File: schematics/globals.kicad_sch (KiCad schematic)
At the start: 35 parts, among them J1 Power, U1 74HCU04, U2 74HC14, U3 ATF22V10C-7, U4 74HC590, U5 74HC590, U6 74HC590, U7 PicoROM32, Y1 12MHz

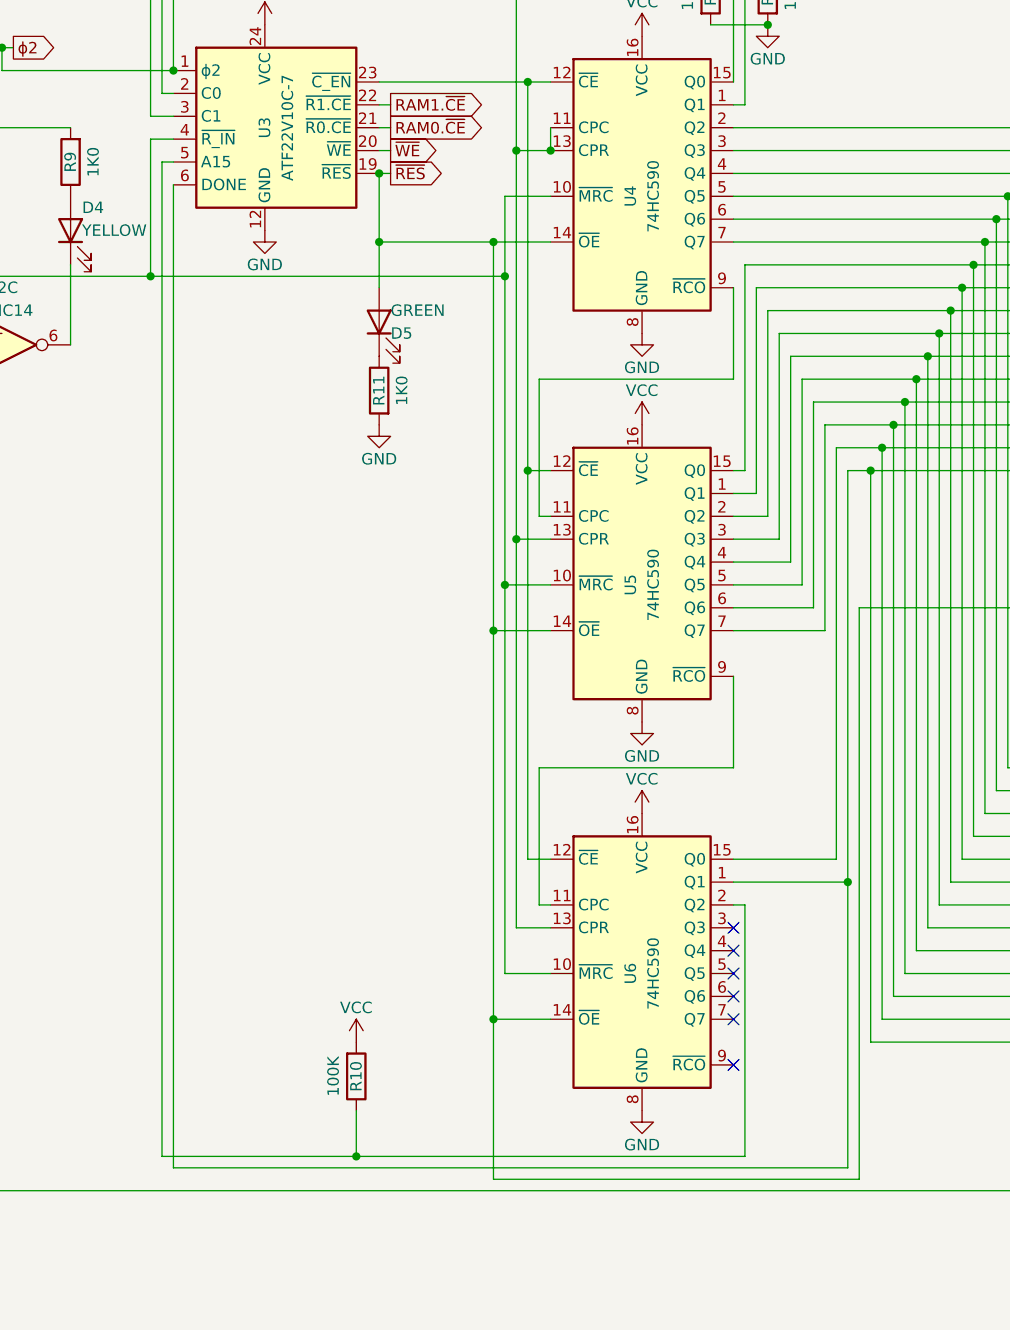
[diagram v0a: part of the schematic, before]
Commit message: forgot bank register transciever so now it's write-only
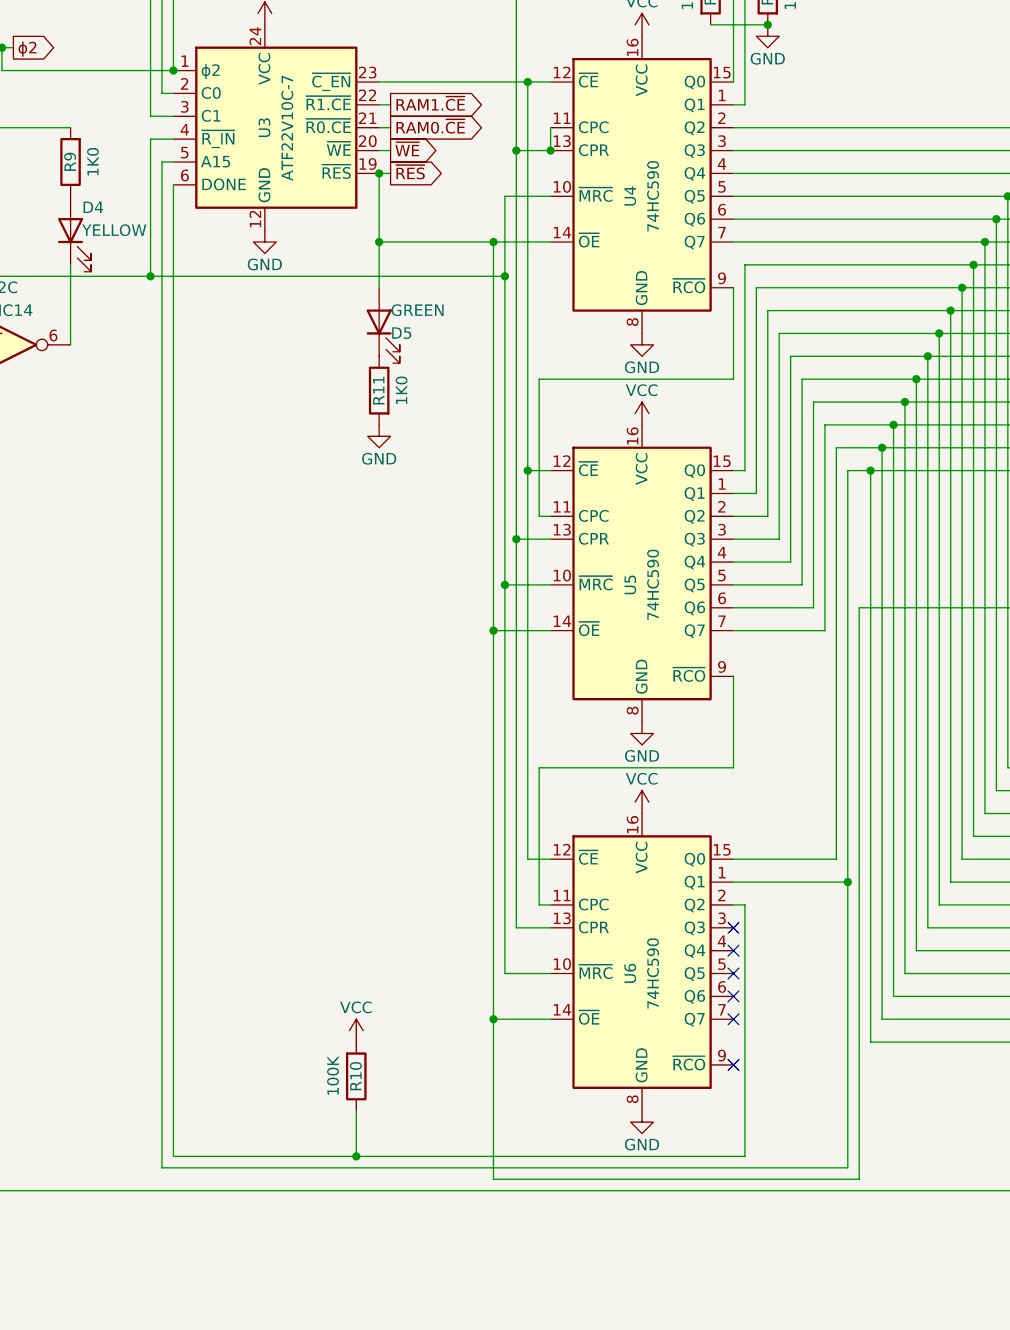
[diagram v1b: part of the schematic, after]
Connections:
- net A15: now also U3.5 (A15); no longer U3.6 (DONE)
- net at R10.1, U6.2 (Q2): now also U3.6 (DONE); no longer U3.5 (A15)
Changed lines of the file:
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@@
 	(wire
 		(pts
-			(xy 116.84 163.83) (xy 191.77 163.83)
+			(xy 115.57 163.83) (xy 191.77 163.83)
 		)
 		(stroke
@@
 	(wire
 		(pts
-			(xy 116.84 54.61) (xy 116.84 163.83)
-		)
-		(stroke
-			(width 0)
-			(type default)
-		)
-	)
-	(wire
-		(pts
 			(xy 59.69 59.69) (xy 59.69 64.77)
 		)
@@
 	(wire
 		(pts
-			(xy 115.57 52.07) (xy 115.57 162.56)
-		)
-		(stroke
-			(width 0)
-			(type default)
-		)
-	)
-	(wire
-		(pts
 			(xy 156.21 86.36) (xy 156.21 43.18)
 		)
@@
 	(wire
 		(pts
+			(xy 115.57 52.07) (xy 116.84 52.07)
+		)
+		(stroke
+			(width 0)
+			(type default)
+		)
+	)
+	(wire
+		(pts
 			(xy 55.88 95.25) (xy 62.23 95.25)
 		)
@@
 	(wire
 		(pts
+			(xy 115.57 52.07) (xy 115.57 163.83)
+		)
+		(stroke
+			(width 0)
+			(type default)
+		)
+	)
+	(wire
+		(pts
 			(xy 191.77 86.36) (xy 194.31 86.36)
 		)
@@
 	(wire
 		(pts
-			(xy 115.57 162.56) (xy 137.16 162.56)
+			(xy 116.84 162.56) (xy 137.16 162.56)
 		)
 		(stroke
@@
 	(wire
 		(pts
+			(xy 116.84 54.61) (xy 116.84 162.56)
+		)
+		(stroke
+			(width 0)
+			(type default)
+		)
+	)
+	(wire
+		(pts
 			(xy 189.23 104.14) (xy 189.23 81.28)
 		)
@@
 		)
 		(stroke
-			(width 0)
-			(type default)
-		)
-	)
-	(wire
-		(pts
-			(xy 116.84 52.07) (xy 115.57 52.07)
-		)
-		(stroke

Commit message: fixing wiring
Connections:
- net A15: now also U3.10 (A15); no longer U3.5 (A15)
- net RAM0.~{CE}: now also U3.16 (R0.~{CE}); no longer U3.21 (~{R0.CE})
- net RAM1.~{CE}: now also U3.17 (R1.~{CE}); no longer U3.22 (~{R1.CE})
- net ~{RES}: now also U3.14 (~{RES}), U3.21
- net ~{WE}: now also U3.15 (~{WE}); no longer U3.20 (~{WE})
- net at R12.1, U4.15 (Q0): now also U3.8 (C0); no longer U3.2 (C0)
- net at R13.1, U4.1 (Q1): now also U3.9 (C1); no longer U3.3 (C1)
- net at D3.2 (A), R6.1, U2.5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: now also U3.7 (~{R_IN}); no longer U3.4 (~{R_IN})
- net at U4.12 (~{CE}), U5.12 (~{CE}), U6.12 (~{CE}): now also U3.18 (C.~{EN}); no longer U3.23 (~{C_EN})
- net at U3.11 (DONE): now also R10.1, U6.2 (Q2)
- now unconnected: U3.6 (DONE)
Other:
- moved on the sheet: C1, C3, R1, R10, R2, R7, R8, U1A, U1B, U1C, U1D, U2A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

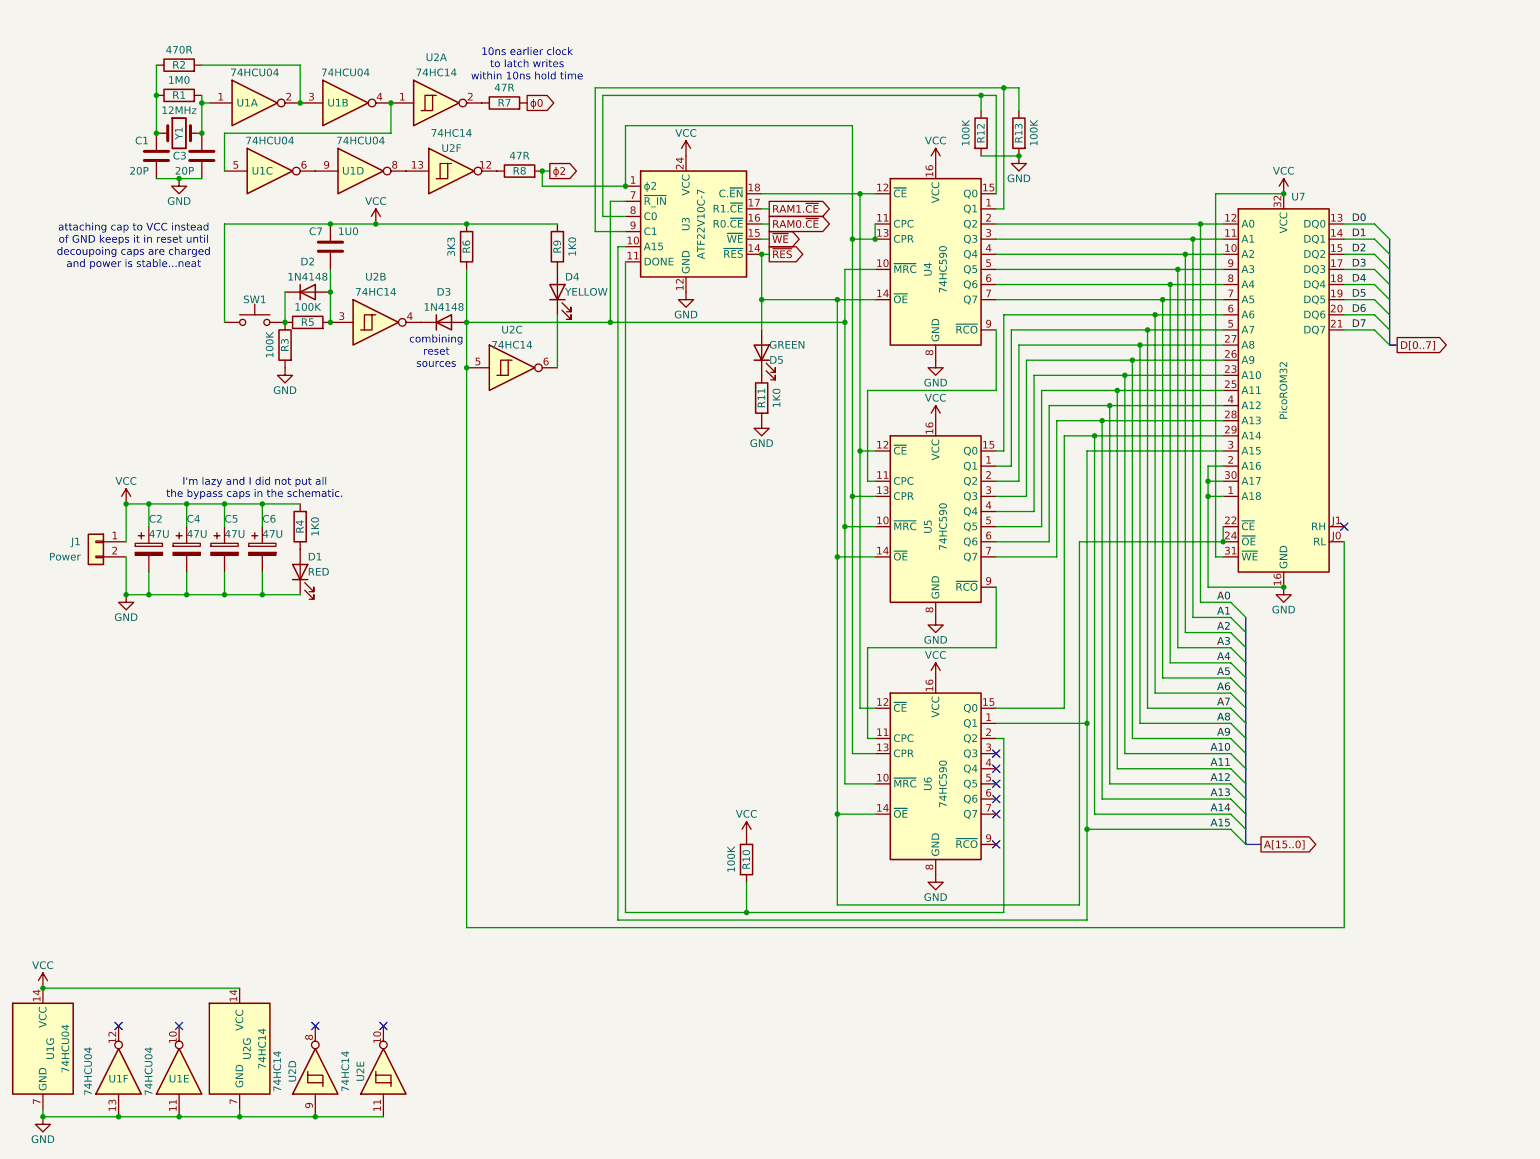
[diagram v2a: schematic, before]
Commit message: combined reset inputs in the pld
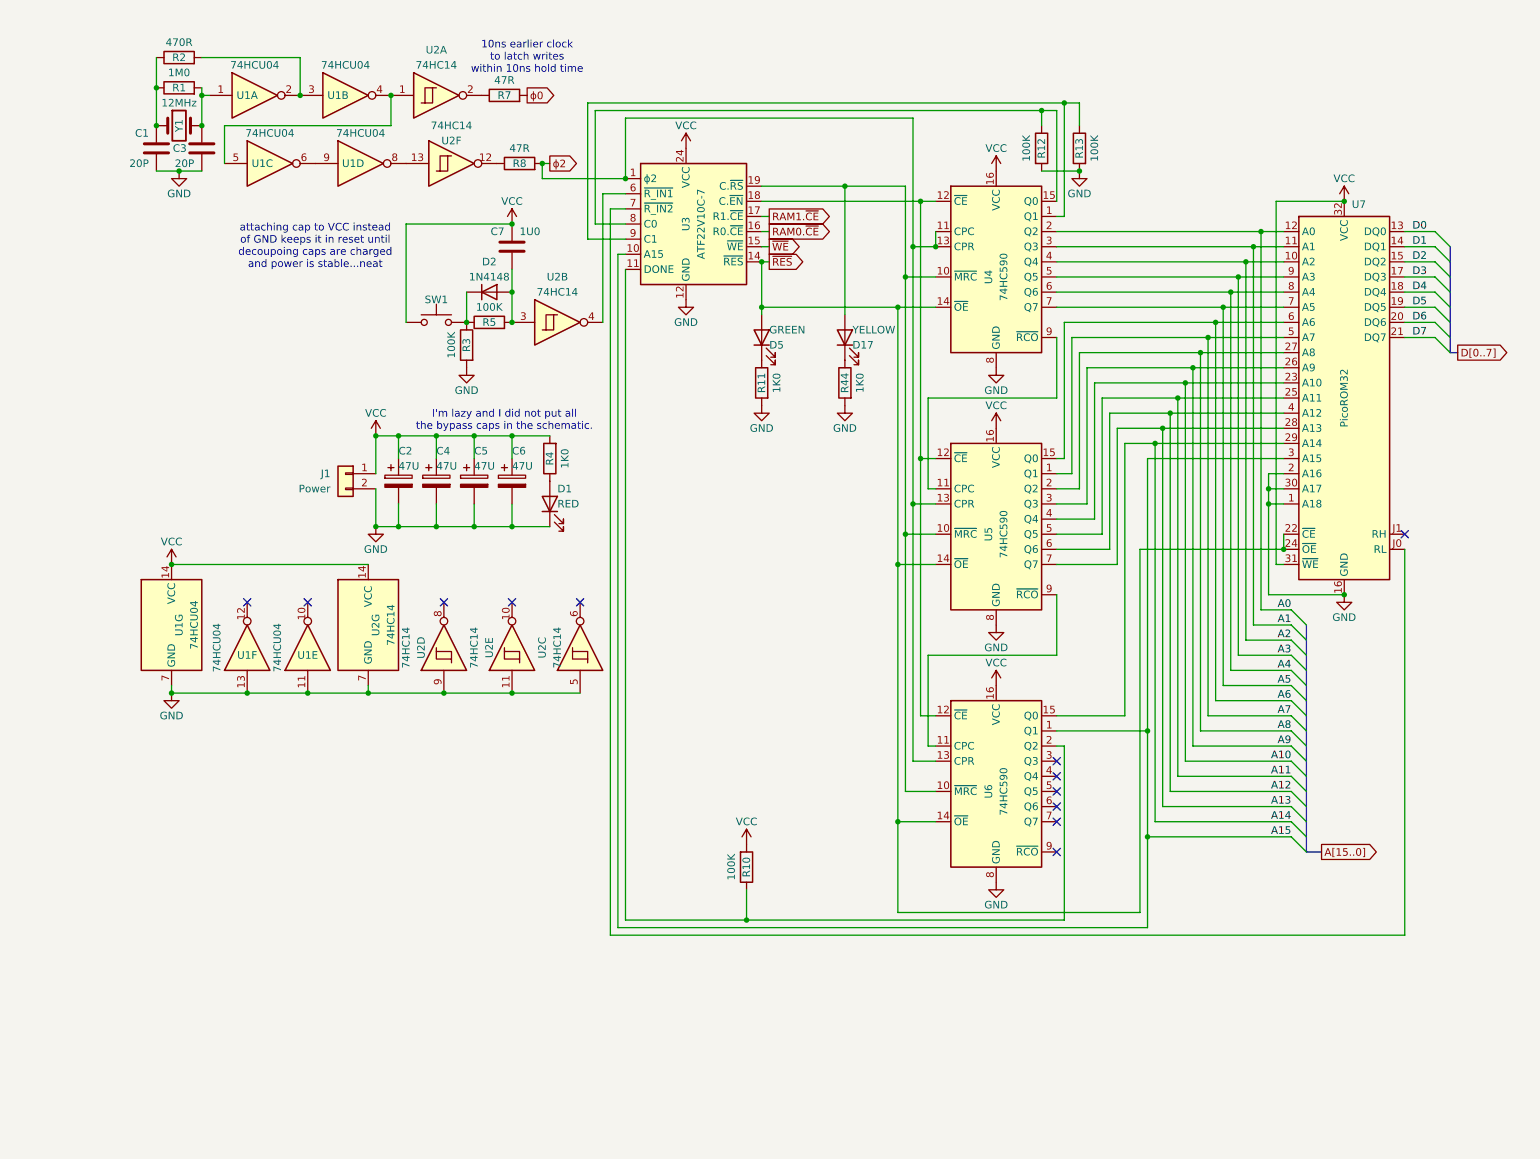
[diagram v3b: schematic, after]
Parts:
- removed D3: 1N4148, Diode_THT:D_DO-35_SOD27_P7.62mm_Horizontal, symbol Diode:1N4148
- removed D4: YELLOW, symbol Device:LED
- removed R6: 3K3, symbol Device:R
- removed R9: 1K0, symbol Device:R
- added D17: YELLOW, symbol Device:LED
- added R44: 1K0, symbol Device:R
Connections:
- net GND: now also U2.5, R44.2
- net ~{RES}: no longer U3.19
- net at U4.10 (~{MRC}), U5.10 (~{MRC}), U6.10 (~{MRC}): now also U3.19 (C.~{RS}), D17.2 (A); no longer U2.5, U3.7 (~{R_IN}), U7.J0 (RL)
- net at U2.4: now also U3.6 (~{R_IN1})
- new net: D17.1 (K), R44.1
- new net: U3.7 (~{R_IN2}), U7.J0 (RL)
- no-connect marks 11 -> 12
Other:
- note removed: "combining reset sources"
- moved on the sheet: C1, C2, C3, C4, C5, C6, C7, D1, D2, D5, J1, R1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

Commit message: my keyboard needed a transceiver after all :(
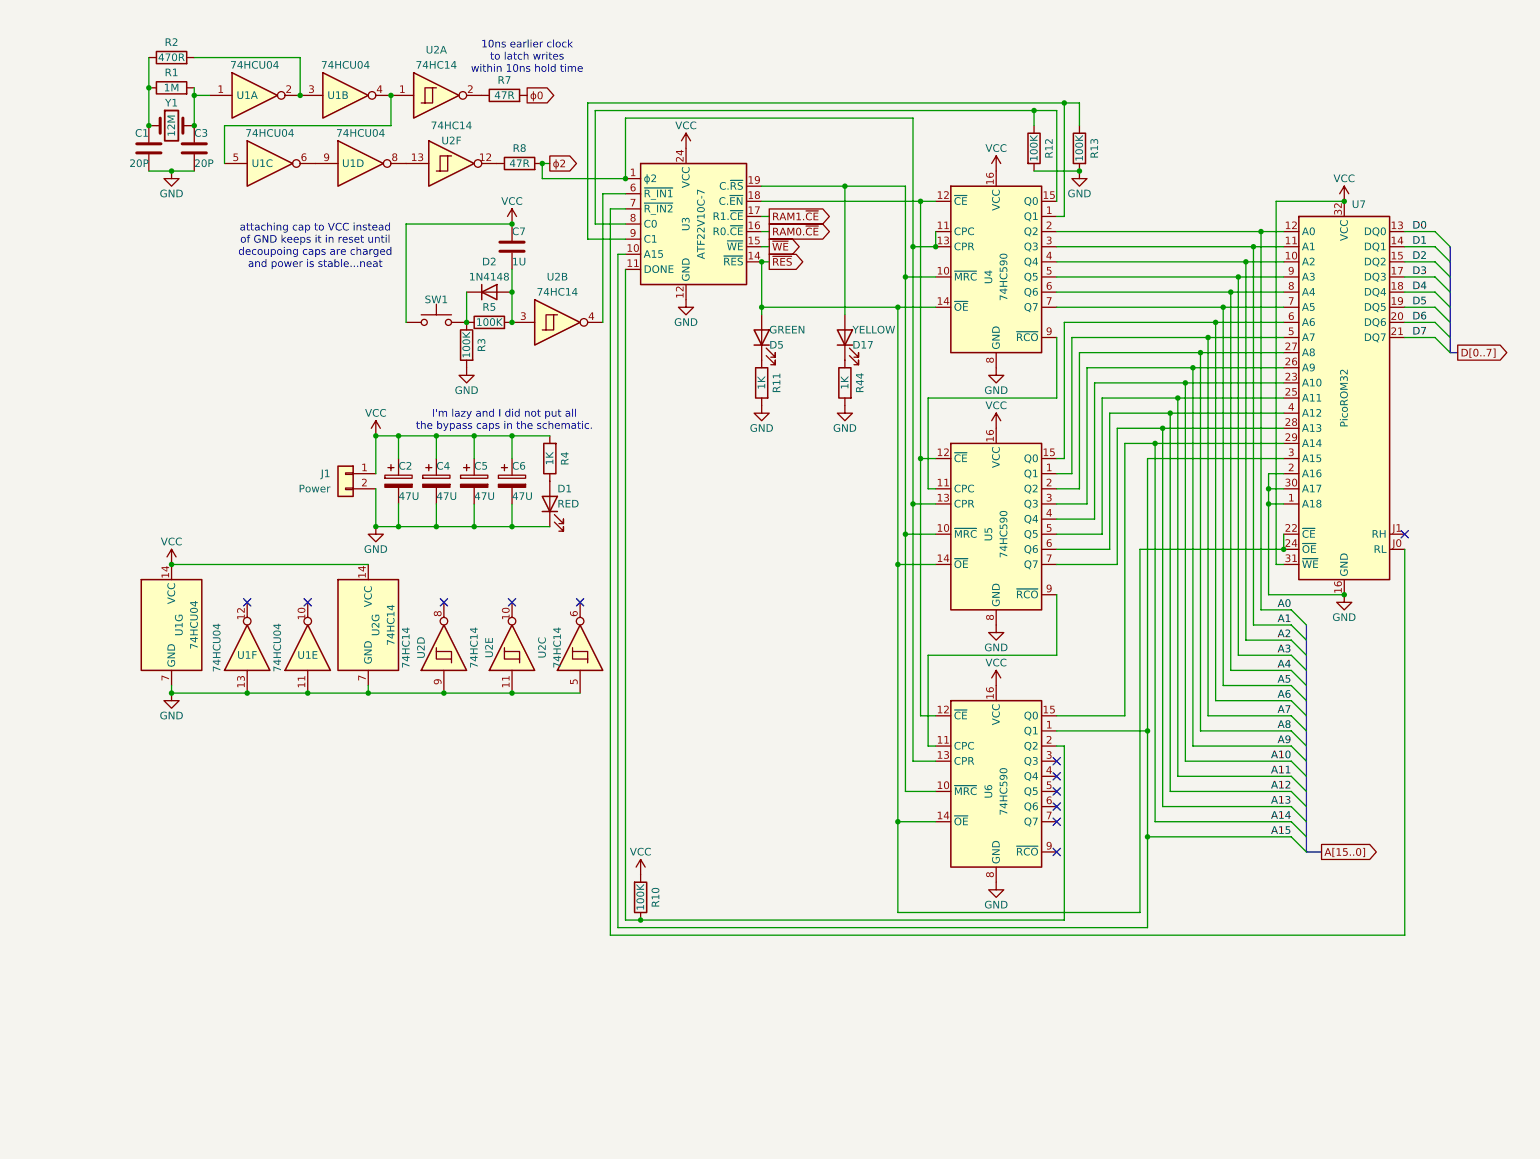
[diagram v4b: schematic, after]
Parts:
- C7: value 1U0 -> 1U
- R1: value 1M0 -> 1M
- R11, R4, R44: value 1K0 -> 1K
- Y1: value 12MHz -> 12M
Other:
- moved on the sheet: C1, C3, R1, R10, R12, R2, Y1
